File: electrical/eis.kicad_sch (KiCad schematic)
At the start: 10 parts

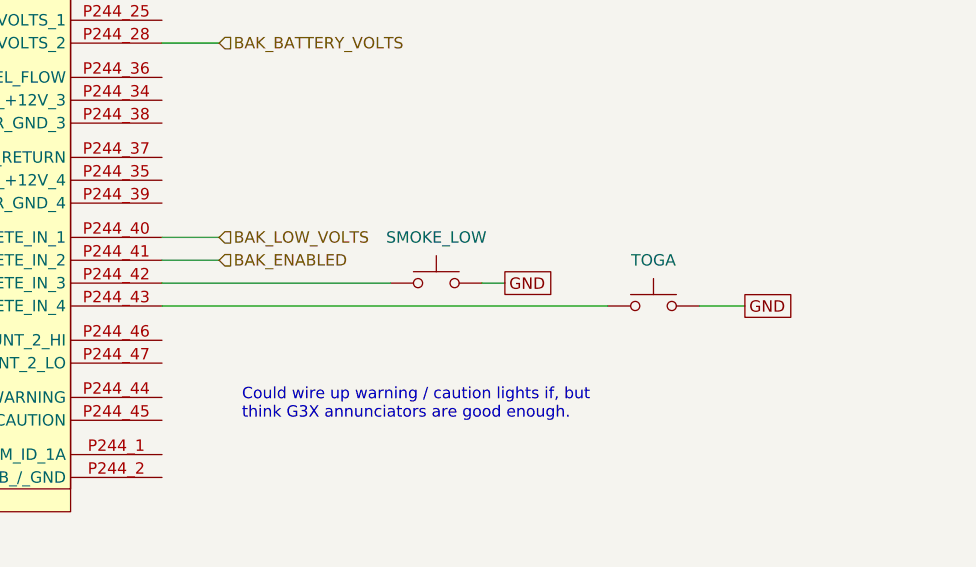
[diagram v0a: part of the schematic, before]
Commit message: Added smoke signal to GEA 24 and moved TOGA to GAD 27
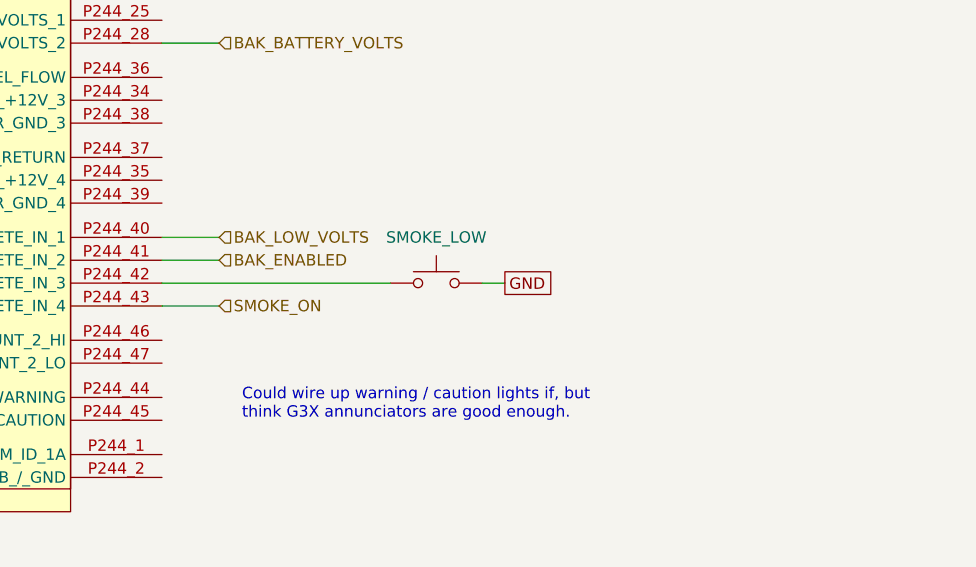
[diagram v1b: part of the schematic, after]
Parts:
- removed TOGA: FLOAT_SENSOR, symbol Switch:SW_Push
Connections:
- net SMOKE_ON: now reaches GEA24.P244_43 (DISCRETE_IN_4)
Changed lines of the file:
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@@
-    (stroke (width 0) (type default))
-  )
-  (wire (pts (xy 67.31 341.63) (xy 116.84 341.63))
     (stroke (width 0) (type default))
   )
@@
     (stroke (width 0) (type default))
   )
+  (wire (pts (xy 67.31 341.63) (xy 73.66 341.63))
+    (stroke (width 0) (type default))
+  )
   (wire (pts (xy 90.17 121.92) (xy 92.71 121.92))
     (stroke (width 0) (type default))
@@
   )
   (wire (pts (xy 83.82 284.48) (xy 83.82 285.75))
-    (stroke (width 0) (type default))
-  )
-  (wire (pts (xy 127 341.63) (xy 132.08 341.63))
     (stroke (width 0) (type default))
   )
@@
     )
   )
-  (global_label "GND" (shape passive) (at 132.08 341.63 0) (fields_autoplaced)
-    (effects (font (size 1.27 1.27)) (justify left))
-    (property "Intersheetrefs" "${INTERSHEET_REFS}" (at 137.8244 341.63 0)
-      (effects (font (size 1.27 1.27)) (justify left) hide)
-    )
-  )
   (hierarchical_label "ROTAX_CAN_B_LO" (shape bidirectional) (at 77.47 227.33 0) (fields_autoplaced)
     (effects (font (size 1.27 1.27)) (justify left))
@@
   )
   (hierarchical_label "CAN_LO_OUT" (shape bidirectional) (at 102.87 40.64 0) (fields_autoplaced)
+    (effects (font (size 1.27 1.27)) (justify left))
+  )
+  (hierarchical_label "SMOKE_ON" (shape input) (at 73.66 341.63 0) (fields_autoplaced)
     (effects (font (size 1.27 1.27)) (justify left))
   )
@@
         )
       )
-    )
-  )
-  (symbol (lib_id "Switch:SW_Push") (at 121.92 341.63 0) (unit 1)
-    (in_bom yes) (on_board yes) (dnp no)
-    (property "Reference" "TOGA" (at 121.92 336.55 0)
-      (effects (font (size 1.27 1.27)))
-    )
-    (property "Value" "FLOAT_SENSOR" (at 121.92 336.55 0)
-      (effects (font (size 1.27 1.27)) hide)
-    )
-    (property "Footprint" "" (at 121.92 336.55 0)
-      (effects (font (size 1.27 1.27)) hide)
-    )
-    (property "Datasheet" "~" (at 121.92 336.55 0)
-      (effects (font (size 1.27 1.27)) hide)
-    )
-    (pin "1")
-    (pin "2")
-    (instances
-      (project "electrical"
-        (path "/e8ec215a-dbe2-4eba-a577-e50a0a128049/72184f52-5cc1-469a-bd6f-4bd63aea59bf"
-          (reference "TOGA") (unit 1)
-        )
-      )

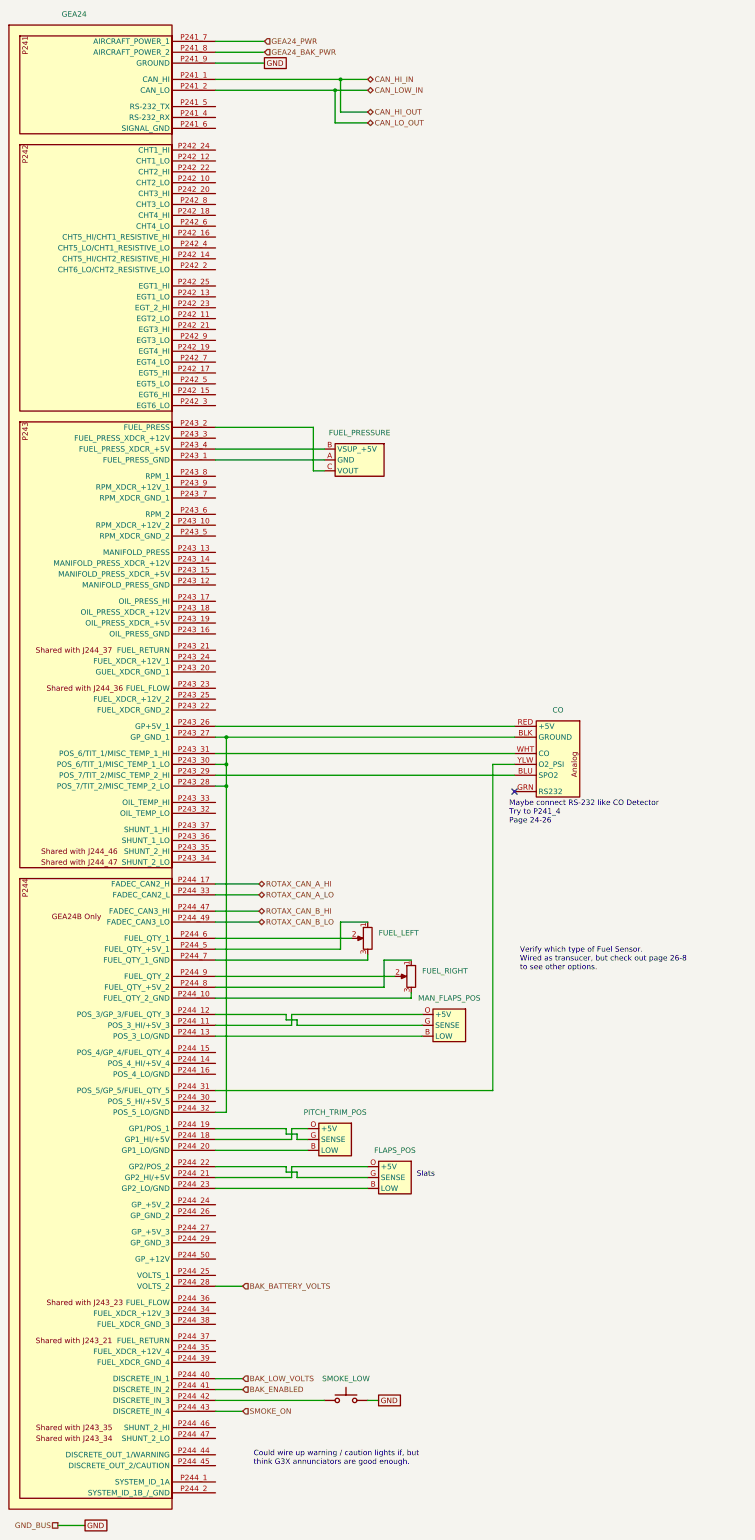
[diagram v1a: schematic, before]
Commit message: Changed grounds and canbuses to be in/out when applicable.
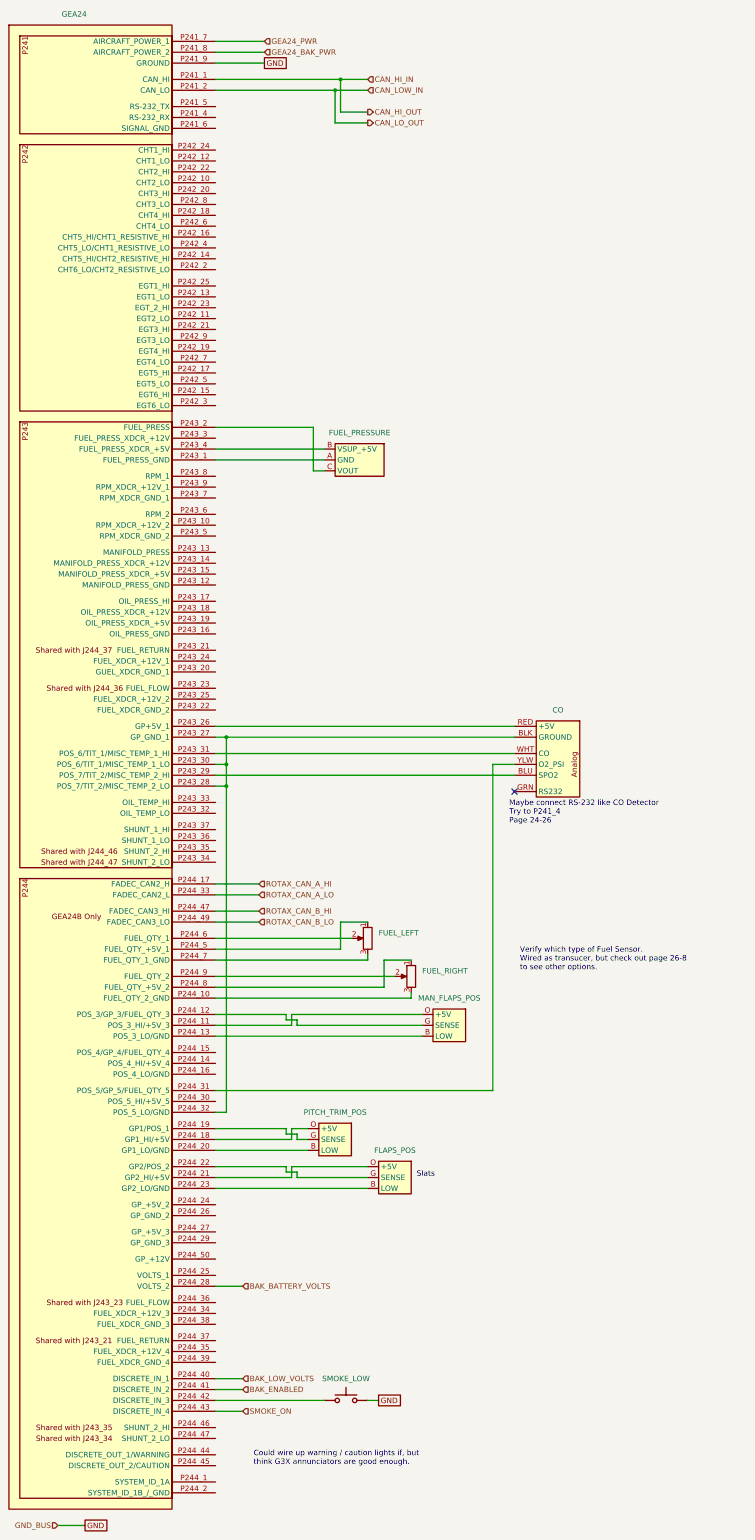
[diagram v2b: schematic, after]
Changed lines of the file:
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@@
     )
   )
-  (hierarchical_label "ROTAX_CAN_B_LO" (shape bidirectional) (at 77.47 227.33 0) (fields_autoplaced)
+  (hierarchical_label "ROTAX_CAN_B_LO" (shape input) (at 77.47 227.33 0) (fields_autoplaced)
     (effects (font (size 1.27 1.27)) (justify left))
   )
@@
     (effects (font (size 1.27 1.27)) (justify left))
   )
-  (hierarchical_label "ROTAX_CAN_B_HI" (shape bidirectional) (at 77.47 224.79 0) (fields_autoplaced)
+  (hierarchical_label "ROTAX_CAN_B_HI" (shape input) (at 77.47 224.79 0) (fields_autoplaced)
     (effects (font (size 1.27 1.27)) (justify left))
   )
-  (hierarchical_label "CAN_LO_OUT" (shape bidirectional) (at 102.87 40.64 0) (fields_autoplaced)
+  (hierarchical_label "CAN_LO_OUT" (shape output) (at 102.87 40.64 0) (fields_autoplaced)
     (effects (font (size 1.27 1.27)) (justify left))
   )
@@
     (effects (font (size 1.27 1.27)) (justify left))
   )
-  (hierarchical_label "ROTAX_CAN_A_HI" (shape bidirectional) (at 77.47 218.44 0) (fields_autoplaced)
+  (hierarchical_label "ROTAX_CAN_A_HI" (shape input) (at 77.47 218.44 0) (fields_autoplaced)
     (effects (font (size 1.27 1.27)) (justify left))
   )
-  (hierarchical_label "CAN_HI_IN" (shape bidirectional) (at 102.87 30.48 0) (fields_autoplaced)
+  (hierarchical_label "CAN_HI_IN" (shape input) (at 102.87 30.48 0) (fields_autoplaced)
     (effects (font (size 1.27 1.27)) (justify left))
   )
@@
     (effects (font (size 1.27 1.27)) (justify left))
   )
-  (hierarchical_label "CAN_LOW_IN" (shape bidirectional) (at 102.87 33.02 0) (fields_autoplaced)
+  (hierarchical_label "CAN_LOW_IN" (shape input) (at 102.87 33.02 0) (fields_autoplaced)
     (effects (font (size 1.27 1.27)) (justify left))
   )
@@
     (effects (font (size 1.27 1.27)) (justify left))
   )
-  (hierarchical_label "GND_BUS" (shape passive) (at 30.48 368.3 180) (fields_autoplaced)
+  (hierarchical_label "GND_BUS" (shape input) (at 30.48 368.3 180) (fields_autoplaced)
     (effects (font (size 1.27 1.27)) (justify right))
   )
-  (hierarchical_label "ROTAX_CAN_A_LO" (shape bidirectional) (at 77.47 220.98 0) (fields_autoplaced)
+  (hierarchical_label "ROTAX_CAN_A_LO" (shape input) (at 77.47 220.98 0) (fields_autoplaced)
     (effects (font (size 1.27 1.27)) (justify left))
   )
-  (hierarchical_label "CAN_HI_OUT" (shape bidirectional) (at 102.87 38.1 0) (fields_autoplaced)
+  (hierarchical_label "CAN_HI_OUT" (shape output) (at 102.87 38.1 0) (fields_autoplaced)
     (effects (font (size 1.27 1.27)) (justify left))
   )

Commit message: Made minimal, and removed everything not needed. want to add GMC 507 back.
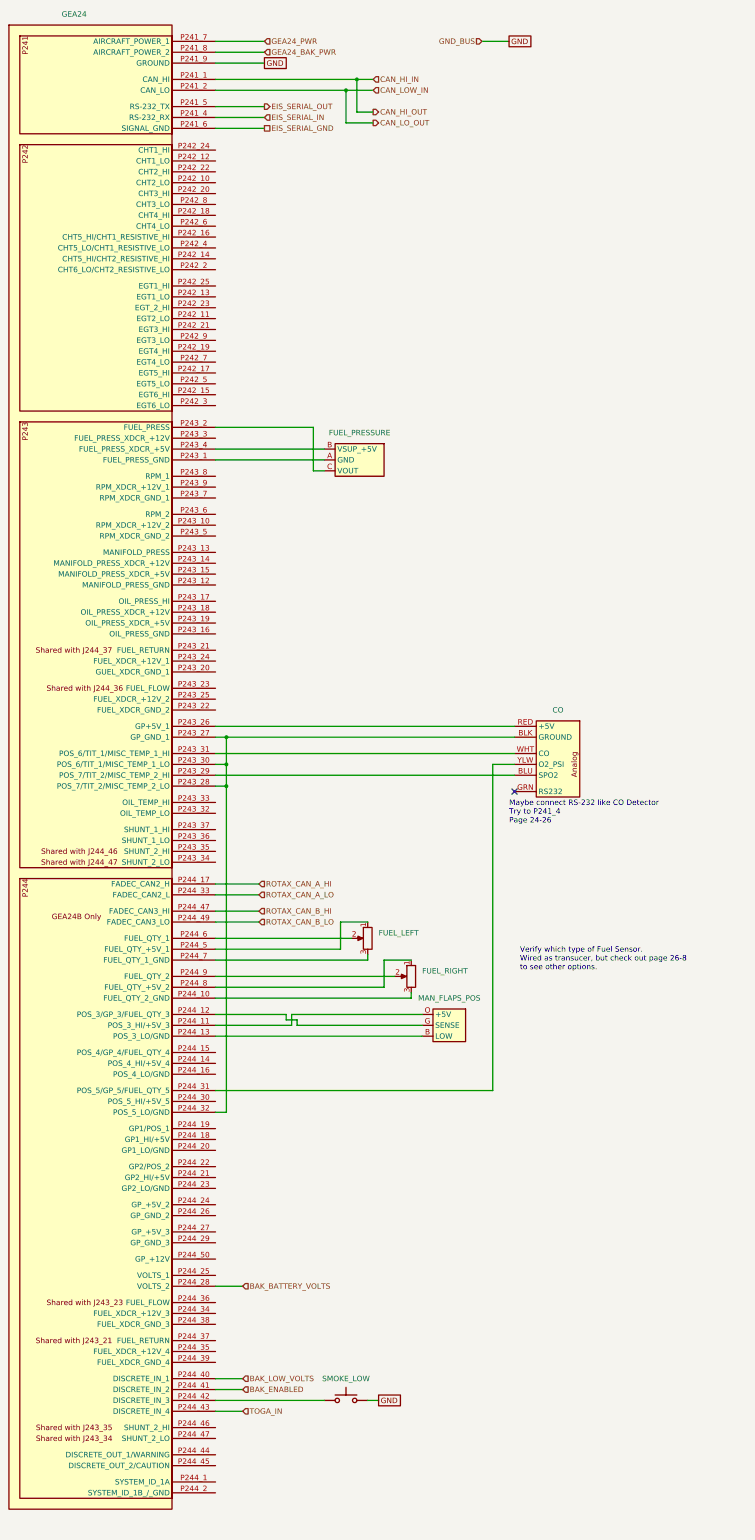
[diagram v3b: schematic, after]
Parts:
- removed FLAPS_POS, PITCH_TRIM_POS: ~, symbol flyerx:Ray_Allen_POS-12
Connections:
- net EIS_SERIAL_IN: now reaches GEA24.P241_4 (RS-232_RX)
- net EIS_SERIAL_OUT: now reaches GEA24.P241_5 (RS-232_TX)
- net EIS_SERIAL_GND: now reaches GEA24.P241_6 (SIGNAL_GND)
- net SMOKE_ON renamed TOGA_IN
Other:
- note removed: "Could wire up warning / caution lights if, but think G3X annunciators are good enough."
- note removed: "Slats"
